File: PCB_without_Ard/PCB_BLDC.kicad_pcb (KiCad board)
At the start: 2 copper layers, 177 x 135.1 mm, 61 parts, among them J1 Power Terminal, J2 Conn_01x03, J3 Conn_01x05, J4 Conn_01x02, J5 Conn_01x04, J6 Conn_01x04, J7 Conn_01x04, J8 Power Terminal, J9 Conn_01x02, Q1 IRF4905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

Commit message: Main: Update Schematic, Add Vias, RC-Filt for Hall-Sense
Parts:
- added C26: 1nF, Capacitor_SMD:C_1206_3216Metric_Pad1.33x1.80mm_HandSolder, F.Cu at (64.5, 102.9)
- added C27: 1nF, Capacitor_SMD:C_1206_3216Metric_Pad1.33x1.80mm_HandSolder, F.Cu at (97.0, 108.7)
- added C28: 1nF, Capacitor_SMD:C_1206_3216Metric_Pad1.33x1.80mm_HandSolder, F.Cu at (130.8, 108.8)
- added R18: 10k, Resistor_SMD:R_1206_3216Metric_Pad1.30x1.75mm_HandSolder, F.Cu at (69.6, 95.5)
- added R19: 10k, Resistor_SMD:R_1206_3216Metric_Pad1.30x1.75mm_HandSolder, F.Cu at (97.6, 85.9)
- added R20: 10k, Resistor_SMD:R_1206_3216Metric_Pad1.30x1.75mm_HandSolder, F.Cu at (104.4, 78.7)
- C6, C7: value 1uF -> 100nF
- moved J4 20.9 mm to (43.4, 105.3)
- moved C6 12.7 mm to (48.7, 112.3)
- moved C7 12.7 mm to (41.1, 112.3)
- moved SW1 12.7 mm to (42.2, 91.4)
- moved J9 8.20 mm to (51.7, 119.3)
- moved R17 7.28 mm to (48.5, 99.3)
- moved R16 7.25 mm to (41.1, 99.3)
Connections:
- C6 pad 1: Net-(C6-Pad1) -> /Rot_B_Pull_Up
- C7 pad 1: Net-(C7-Pad1) -> /Rot_A_Pull_Up
- J5 pad 1: /L1_Sense -> Net-(C26-Pad1)
- J6 pad 1: /L2_Sense -> Net-(C27-Pad1)
- J7 pad 1: /L3_Sense -> Net-(C28-Pad1)
- R16 pad 1: /Rot_A_Pull_Up -> Net-(R16-Pad1)
- R16 pad 2: Net-(C7-Pad1) -> /Rot_A_Pull_Up
- R17 pad 1: /Rot_B_Pull_Up -> Net-(R17-Pad1)
- R17 pad 2: Net-(C6-Pad1) -> /Rot_B_Pull_Up
- SW1 pad A: /Rot_A_Pull_Up -> Net-(R16-Pad1)
- SW1 pad B: /Rot_B_Pull_Up -> Net-(R17-Pad1)
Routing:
- net Net-(C28-Pad1): track 0.00 -> 56.0 mm, vias 0 -> 3
- net /L3_Sense: track 70.8 -> 17.5 mm, vias 3 -> 0
- net Net-(C27-Pad1): track 0.00 -> 32.3 mm, vias 0 -> 1
- net /L2_Sense: track 47.7 -> 20.7 mm, vias 2 -> 0
- net Net-(C26-Pad1): track 0.00 -> 14.0 mm
- net /L1_Sense: track 31.1 -> 17.6 mm
- net /Rot_B_Pull_Up: track 0.00 -> 12.1 mm
- net /Rot_A_Pull_Up: track 0.00 -> 11.9 mm
- net Net-(R17-Pad1): track 0.00 -> 6.91 mm
- net Net-(R16-Pad1): track 0.00 -> 6.80 mm
- net Net-(C7-Pad1): track 4.49 -> 0.00 mm
- net Net-(C6-Pad1): track 4.49 -> 0.00 mm
- net /VCC_5V: track 75.5 -> 74.6 mm
- net GND: vias 105 -> 83
- net (no net): vias 7 -> 35
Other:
- board size 177 x 135.1 mm -> 141 x 92.7 mm
- board text added: "A | B"
- board text added: "Rotary Encoder"

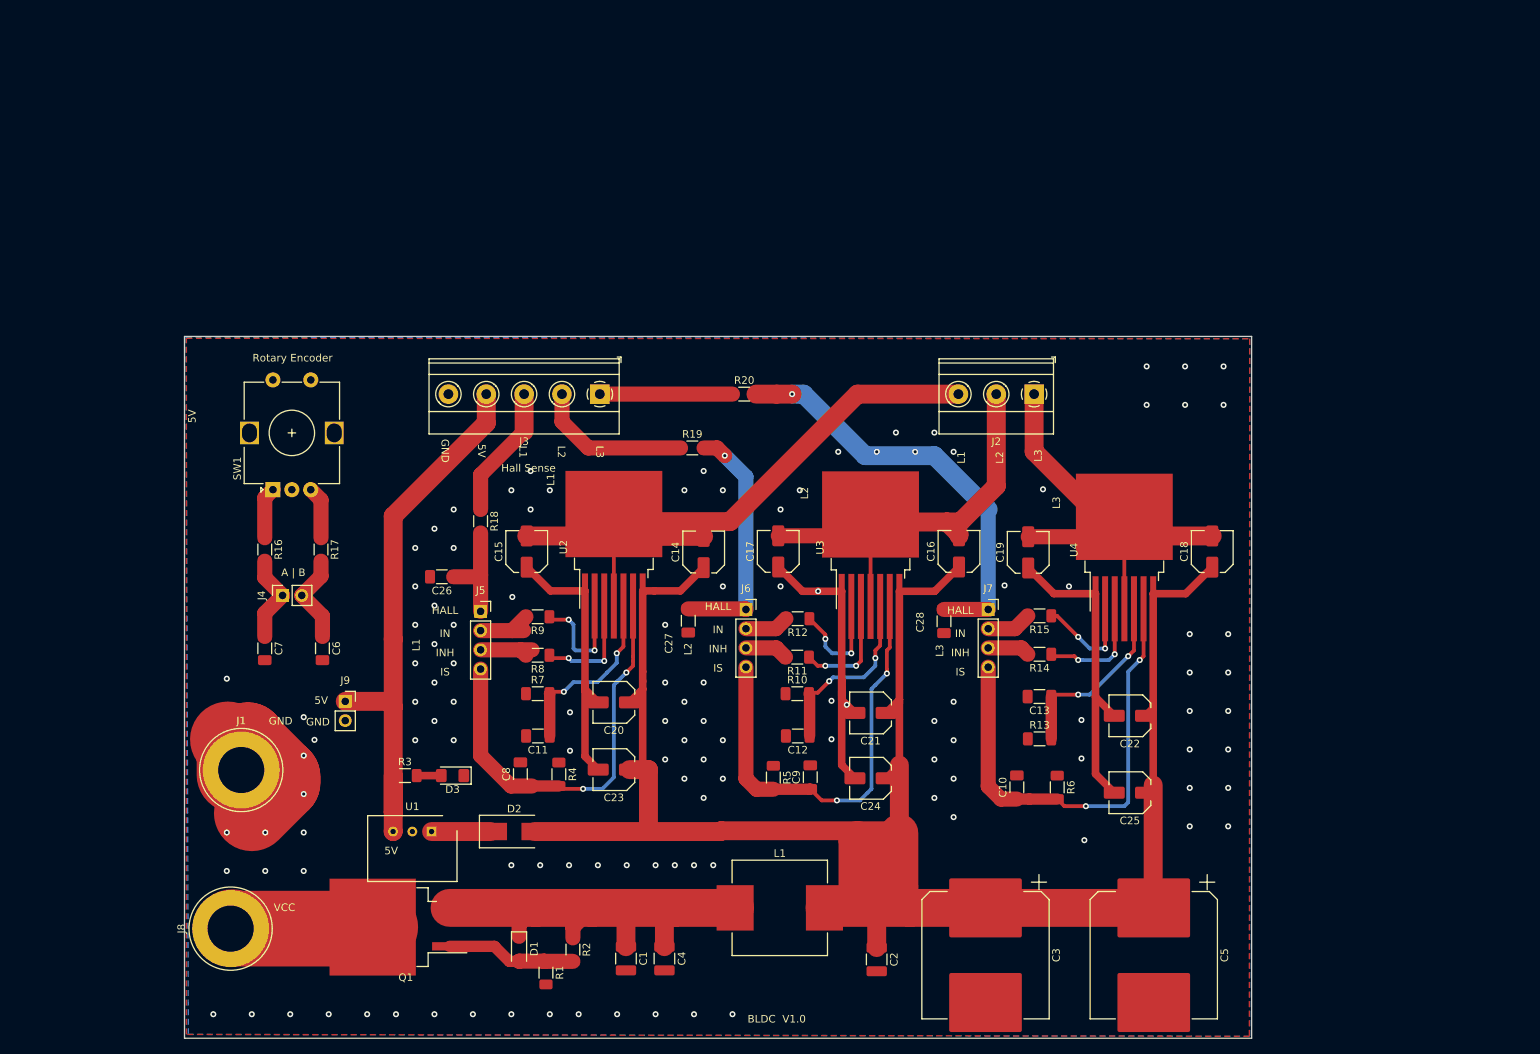
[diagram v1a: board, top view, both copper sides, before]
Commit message: PCB: Fixed again Low Pass Filter
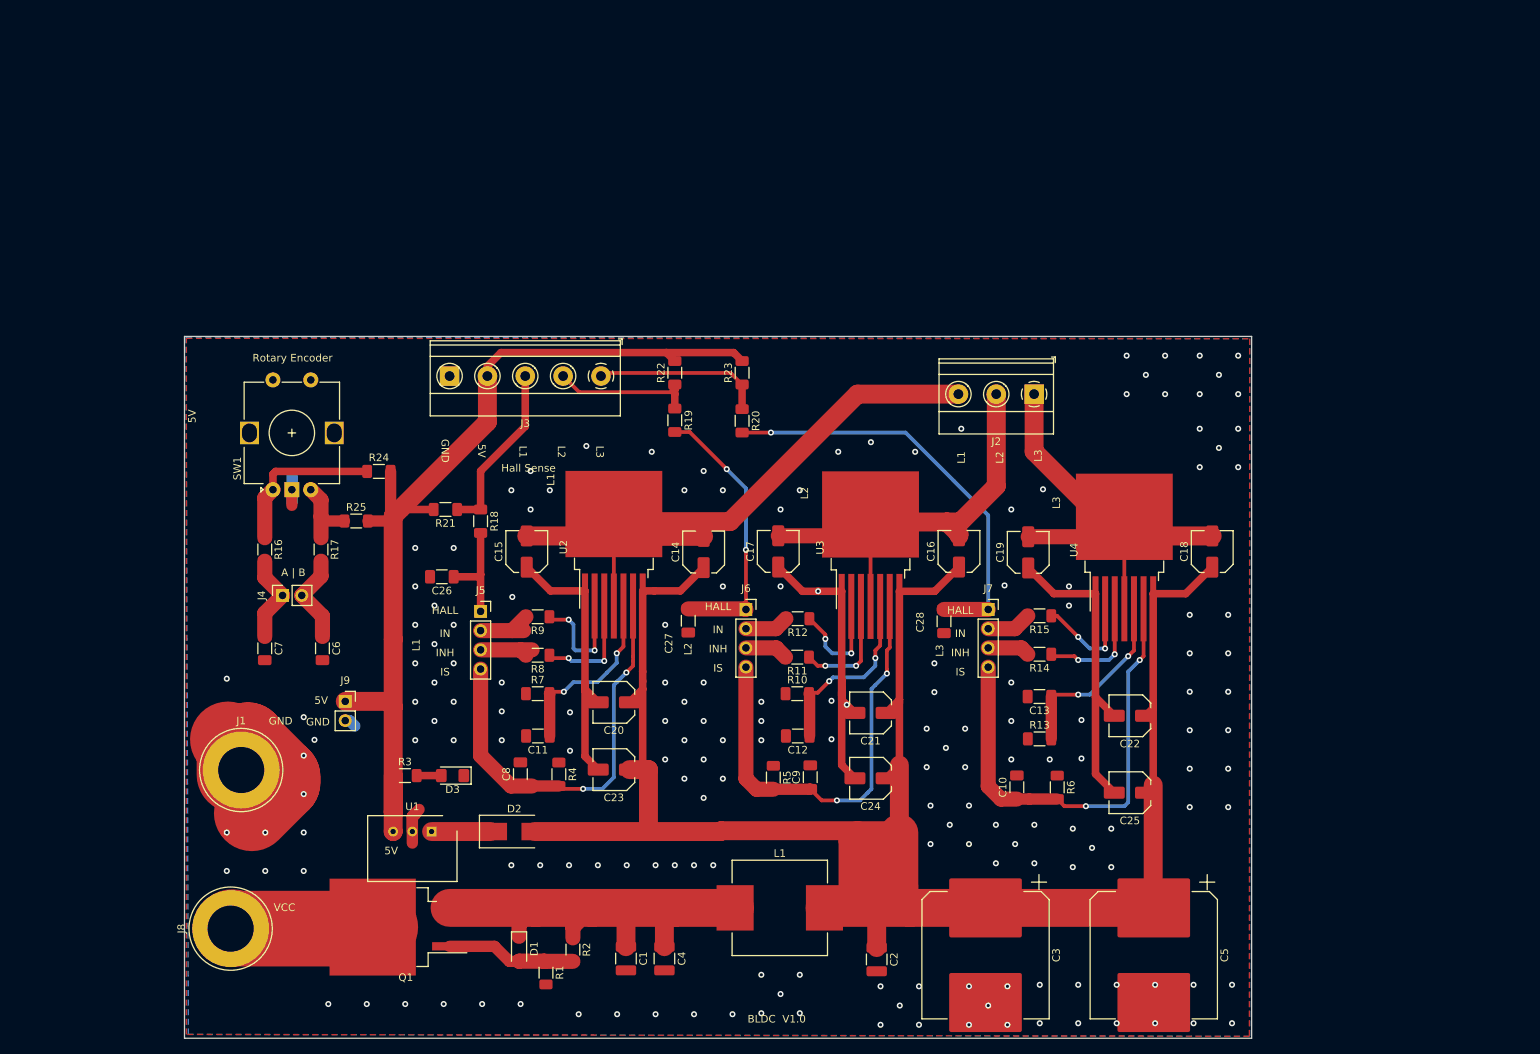
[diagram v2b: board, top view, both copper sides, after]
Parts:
- added R21: 10k, Resistor_SMD:R_1206_3216Metric_Pad1.30x1.75mm_HandSolder, F.Cu at (64.9, 94.0)
- added R22: 10k, Resistor_SMD:R_1206_3216Metric_Pad1.30x1.75mm_HandSolder, F.Cu at (95.2, 75.9)
- added R23: 10k, Resistor_SMD:R_1206_3216Metric_Pad1.30x1.75mm_HandSolder, F.Cu at (104.1, 75.9)
- added R24: 10k, Resistor_SMD:R_1206_3216Metric_Pad1.30x1.75mm_HandSolder, F.Cu at (56.2, 89.0)
- added R25: 10k, Resistor_SMD:R_1206_3216Metric_Pad1.30x1.75mm_HandSolder, F.Cu at (53.2, 95.5)
- J1: value Power Terminal -> Ground Terminal
- moved R19 4.33 mm to (95.2, 82.2), turned to 270 degrees
- moved R20 3.54 mm to (104.1, 82.3), turned to 270 degrees
- moved J3 2.39 mm to (85.5, 76.4)
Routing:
- net /VCC_5V: track 74.6 -> 128.8 mm
- net GND: track 138.7 -> 158.4 mm, vias 83 -> 131
- net Net-(R16-Pad1): track 6.80 -> 21.4 mm
- net /L1_Sense: track 17.6 -> 23.2 mm
- net /L3_Sense: track 17.5 -> 22.6 mm
- net Net-(C27-Pad1): track 32.3 -> 36.1 mm, vias 1 -> 2
- net Net-(R17-Pad1): track 6.91 -> 10.3 mm
- net /L2_Sense: track 20.7 -> 19.3 mm
- net Net-(C28-Pad1): track 56.0 -> 55.3 mm, vias 3 -> 1
- net (no net): vias 35 -> 45

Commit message: PCB: Changed Power Terminals to correct one, Adapted csv-File to PT1-Filter
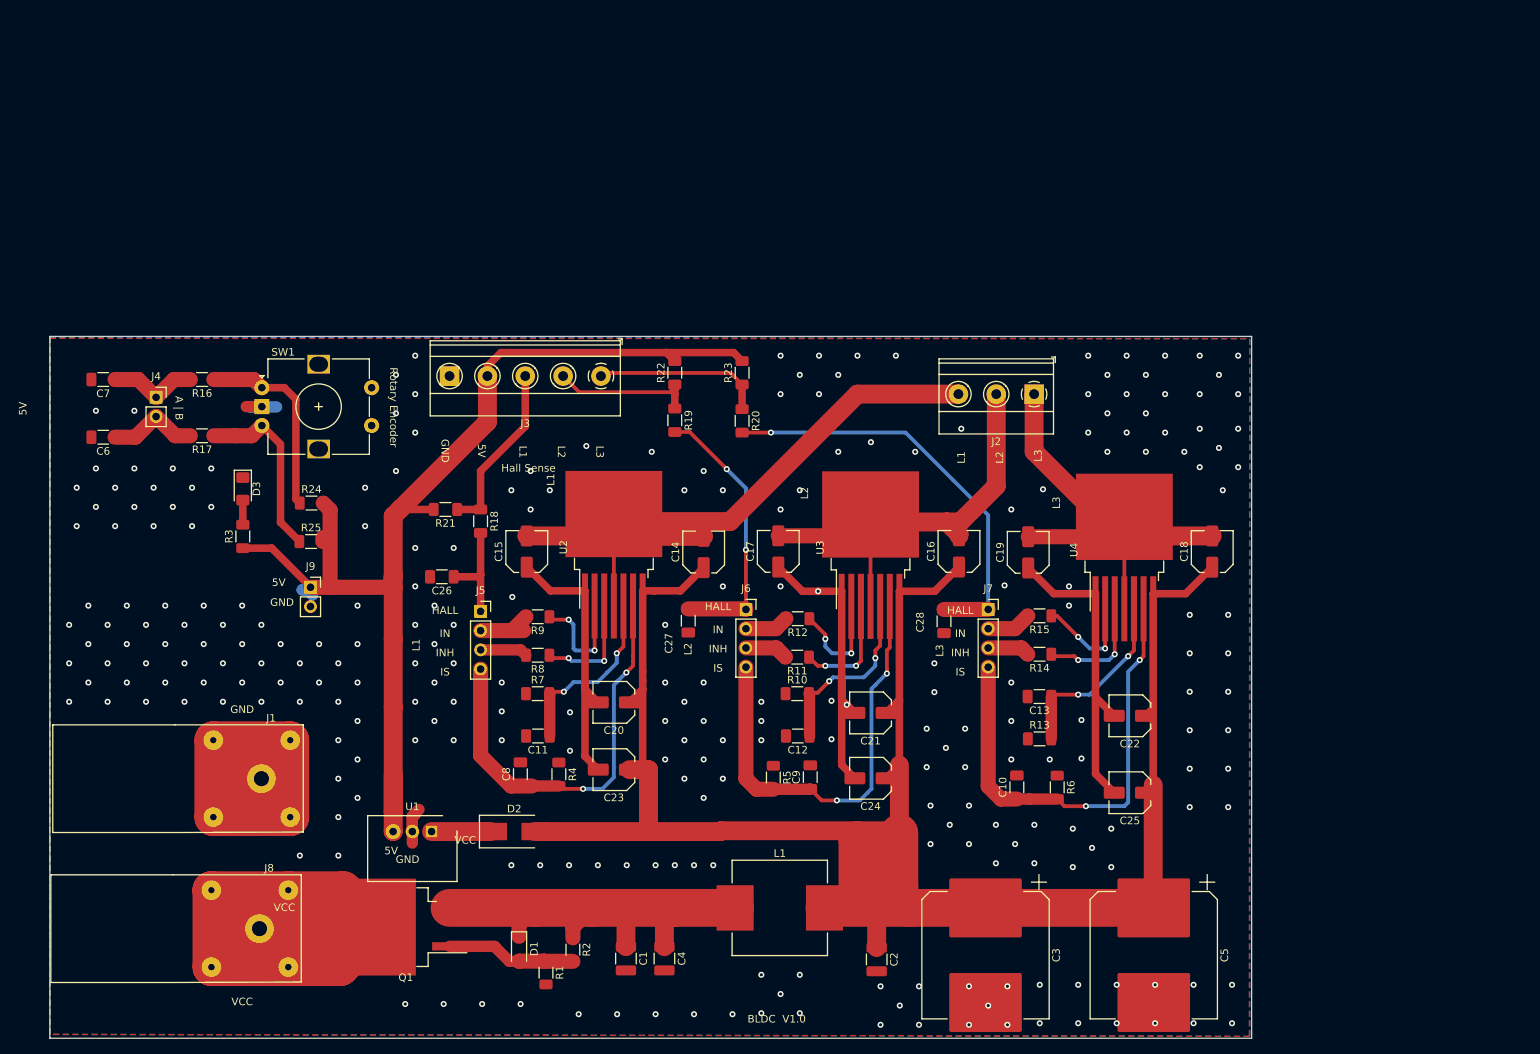
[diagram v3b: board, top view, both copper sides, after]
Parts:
- J1, J8: footprint Connector:Banana_Jack_1Pin -> Connector:CalTest_CT3151
- moved D3 46.9 mm to (38.2, 91.3), turned to 270 degrees
- moved C7 41.4 mm to (19.7, 76.8), turned to 180 degrees
- moved C6 40.2 mm to (19.7, 84.4), turned to 180 degrees
- moved R3 38.2 mm to (38.2, 97.5), turned to 90 degrees
- moved J4 31.0 mm to (26.7, 79.2), turned to 0 degrees
- moved R16 23.9 mm to (32.8, 76.8), turned to 180 degrees
- moved R17 21.7 mm to (32.8, 84.2), turned to 180 degrees
- moved J9 15.8 mm to (47.1, 104.3)
- moved SW1 13.6 mm to (40.7, 77.9), turned to 0 degrees
- moved R24 9.84 mm to (47.3, 93.1)
- moved R25 6.55 mm to (47.2, 98.2)
- moved J8 3.59 mm to (39.1, 146.8), turned to 0 degrees
- moved J1 1.98 mm to (39.4, 127.0)
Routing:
- net /VCC_Unregulated: track 20.1 -> 82.1 mm
- net /VCC_5V: track 128.8 -> 149.5 mm
- net GND: track 158.4 -> 177.8 mm, vias 131 -> 261
- net Net-(R17-Pad1): track 10.3 -> 24.3 mm
- net Net-(R16-Pad1): track 21.4 -> 25.9 mm
- net /L1_INH: track 7.81 -> 6.29 mm
- net (no net): vias 45 -> 0
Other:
- board size 141 x 92.7 mm -> 158.8 x 92.7 mm

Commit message: Minor adjustments @ THT size  csv and resistor values
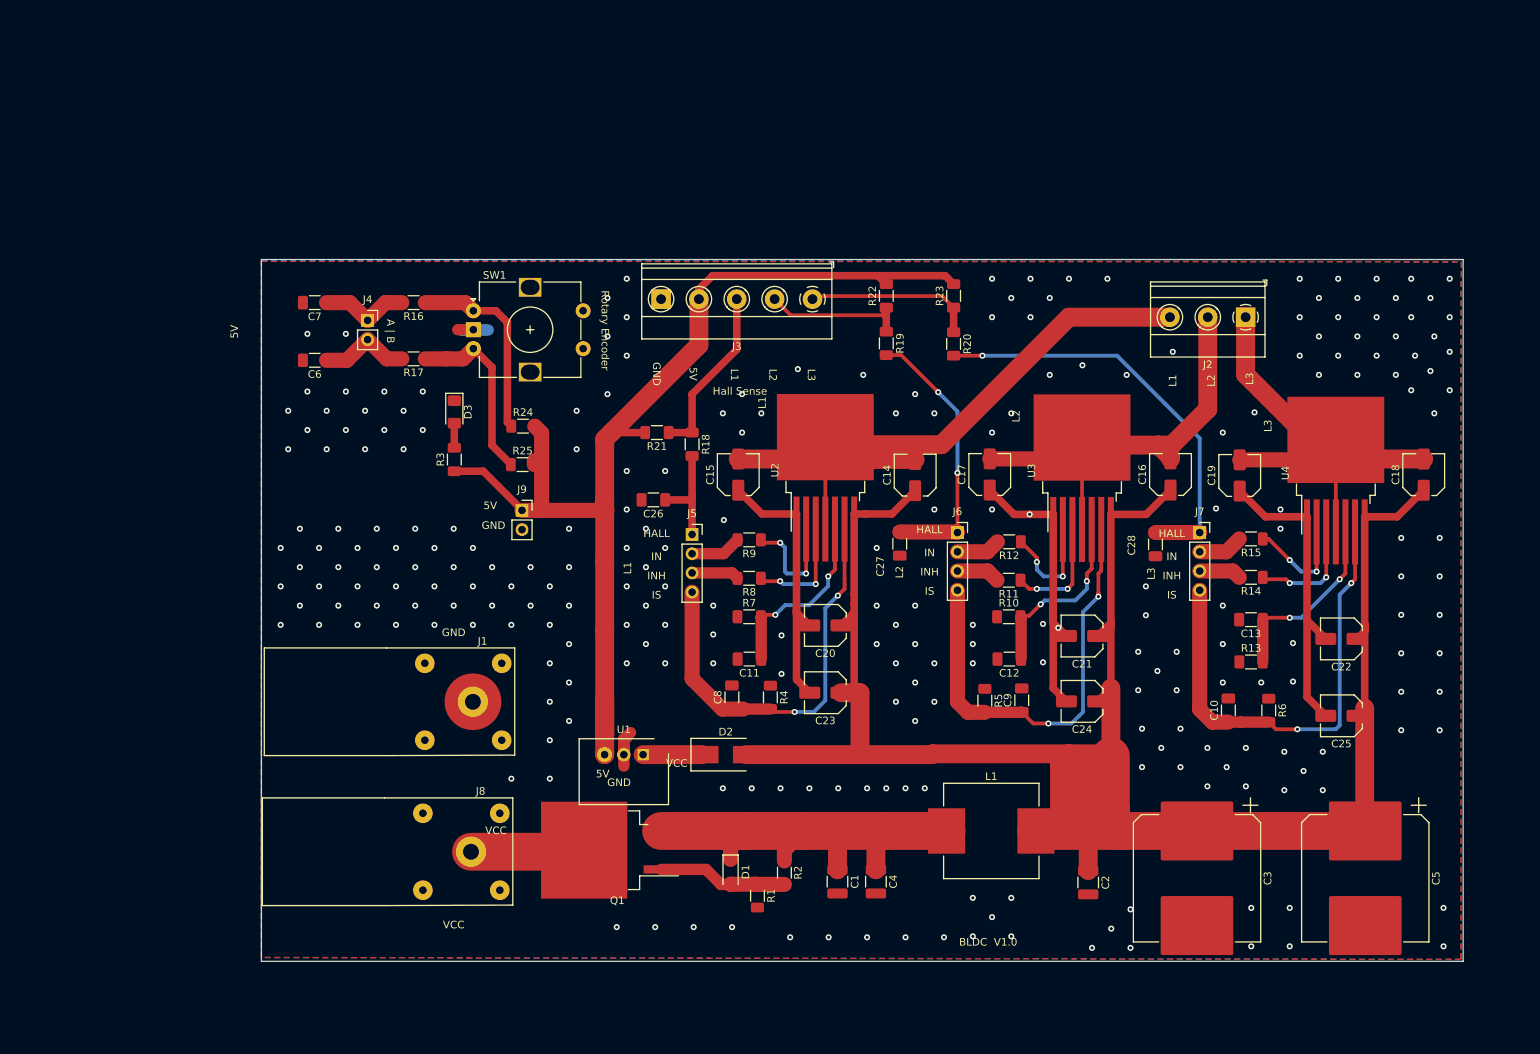
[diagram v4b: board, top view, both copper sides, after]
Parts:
- moved J7 29.7 mm to (164.6, 97.0)
- moved C15 29.7 mm to (103.6, 89.4)
- moved C2 29.7 mm to (149.9, 143.3)
- moved C9 29.7 mm to (141.1, 119.2)
- moved J3 29.7 mm to (113.4, 66.2)
- moved J8 29.7 mm to (67.1, 136.7)
- moved L1 29.7 mm to (137.1, 136.4)
- moved R10 29.7 mm to (139.4, 108.2)
- moved R11 29.7 mm to (139.4, 103.3)
- moved R17 29.7 mm to (60.7, 74.1)
- moved R20 29.7 mm to (132.1, 72.1)
- moved R23 29.7 mm to (132.1, 65.8)
- moved R24 29.7 mm to (75.2, 83.0)
- moved R3 29.7 mm to (66.1, 87.4)
- moved R5 29.7 mm to (136.2, 119.2)
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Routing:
- net /VCC_Unregulated: track 82.1 -> 16.0 mm
- net GND: track 177.8 -> 136.7 mm, vias 261 -> 251
- net /VCC_5V: track 149.5 -> 147.8 mm
- net /L1_IN: track 8.27 -> 6.75 mm
